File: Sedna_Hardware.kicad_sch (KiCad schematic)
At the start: 24 parts, among them U1 LD1117V33, U2 ESP32-WROOM-32E

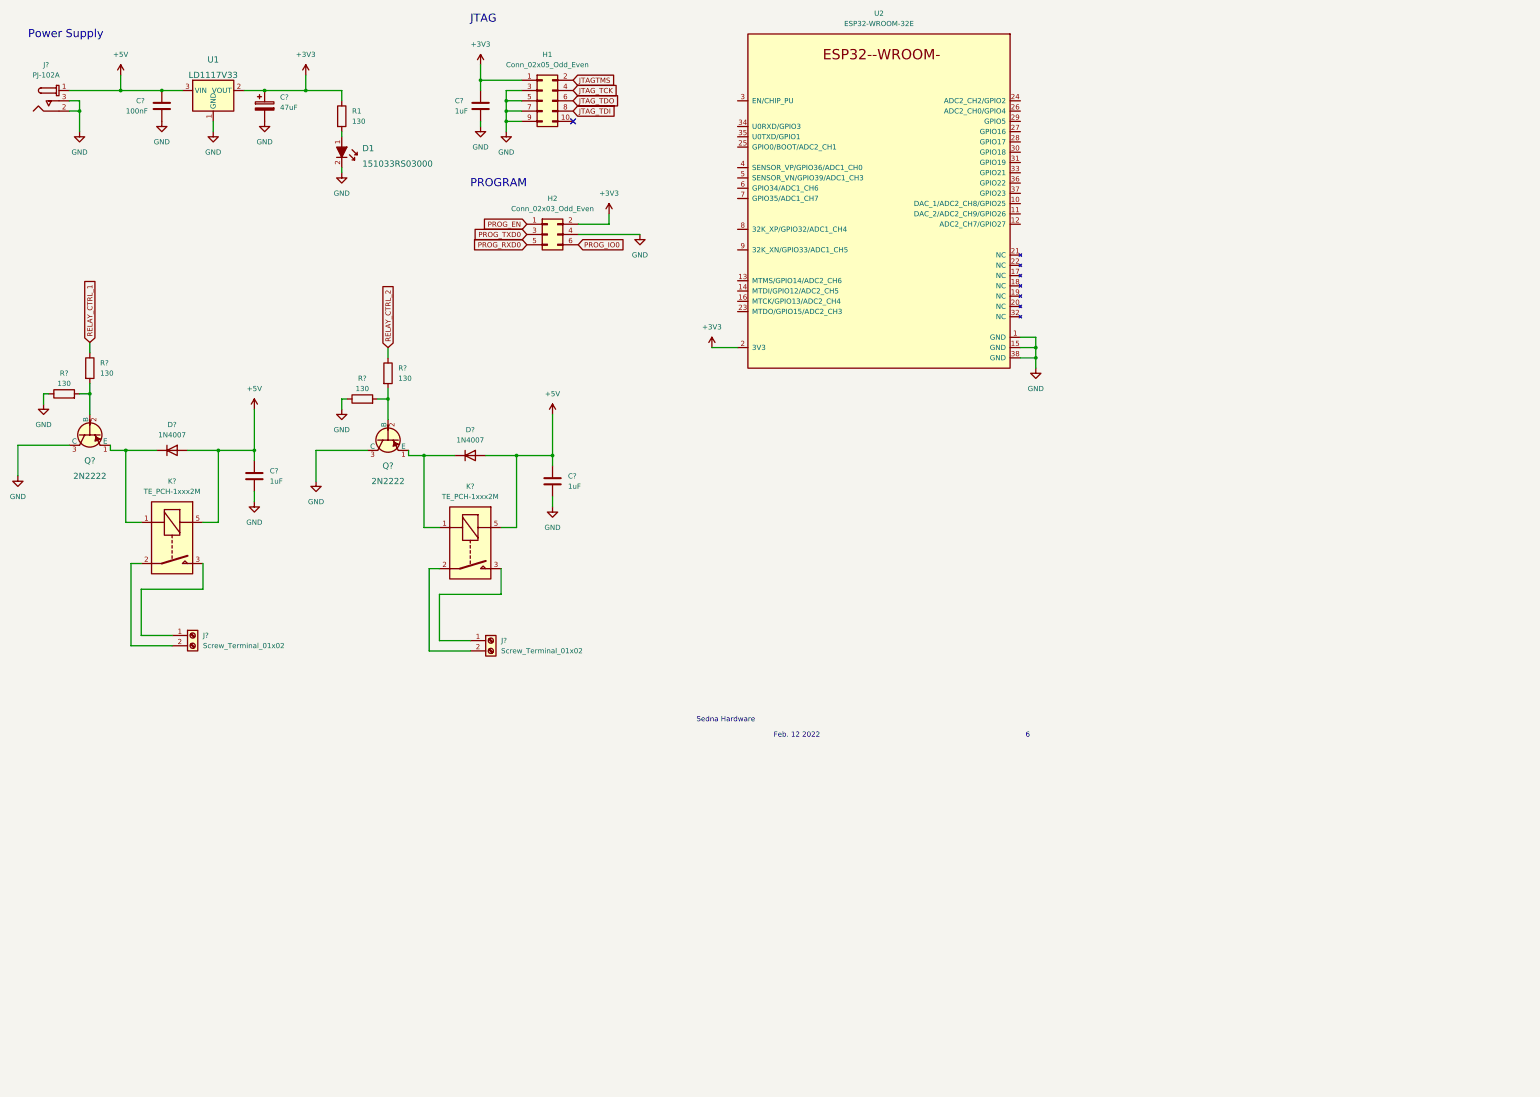
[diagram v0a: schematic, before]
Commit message: Added various headers for sensors, servo, led strips, etc.
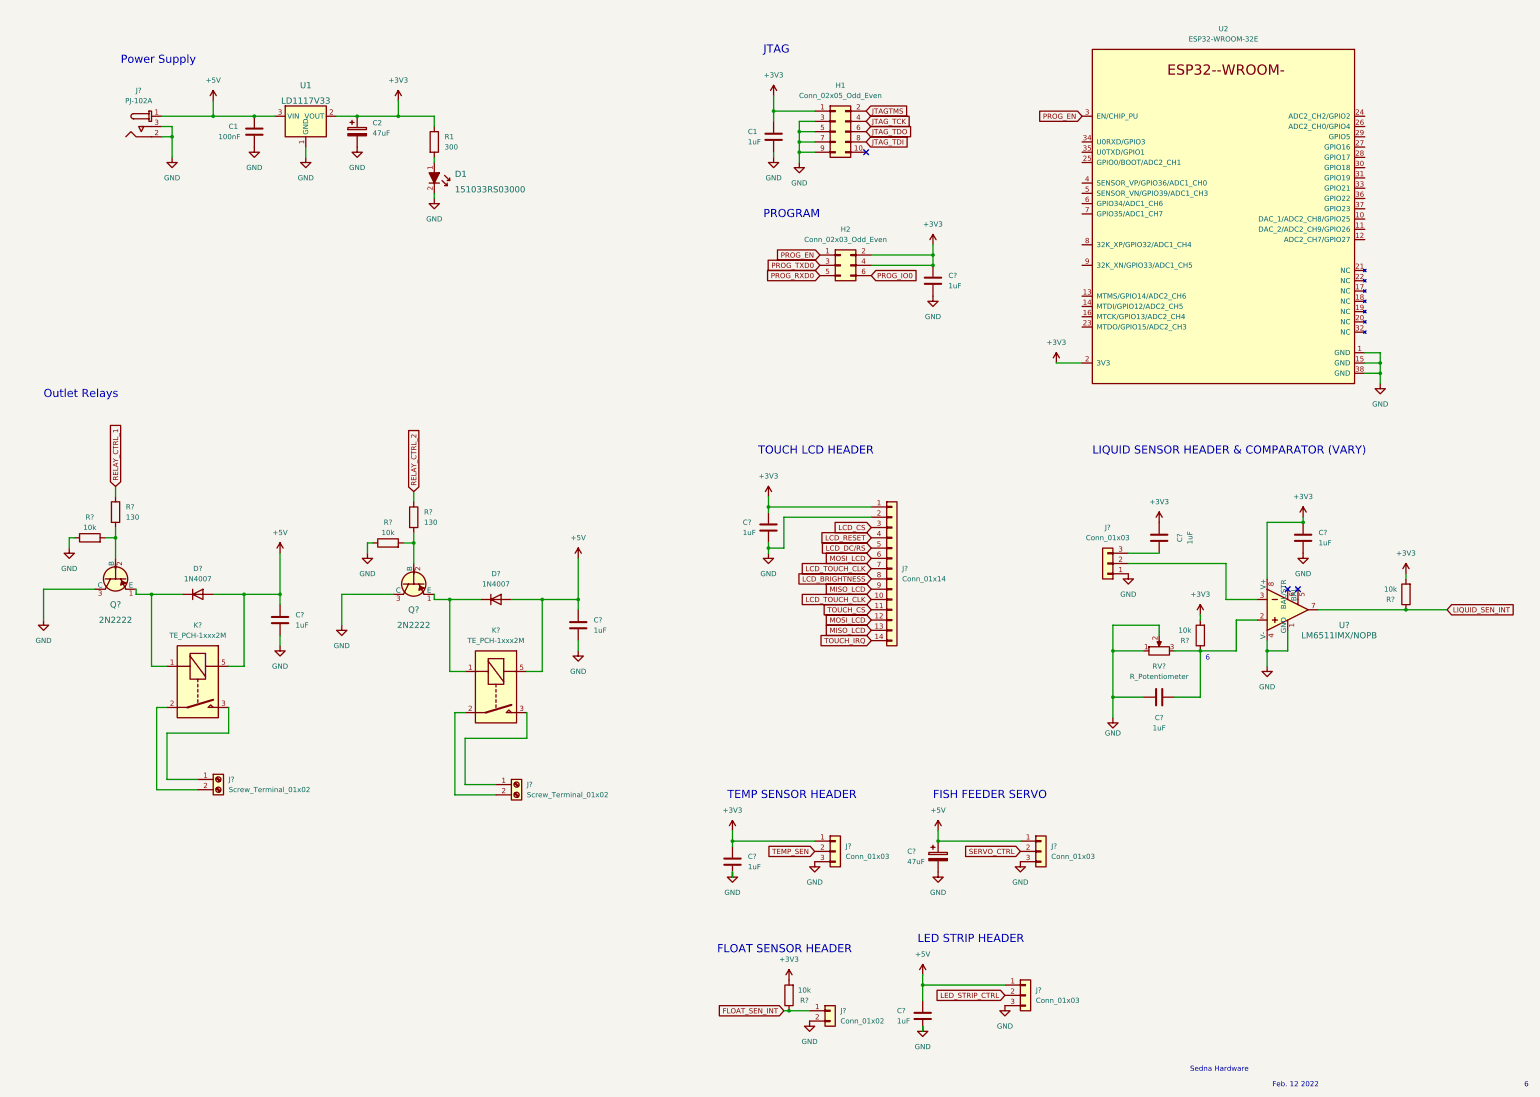
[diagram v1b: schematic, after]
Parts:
- added C? (x7): 1uF, symbol Device:C
- added C?: 47uF, symbol Device:C_Polarized
- added J?: Conn_01x02, symbol Connector_Generic:Conn_01x02
- added J? (x4): Conn_01x03, symbol Connector_Generic:Conn_01x03
- added J?: Conn_01x14, symbol Connector_Generic:Conn_01x14
- added R? (x3): 10k, symbol Device:R
- added RV?: R_Potentiometer, symbol Device:R_Potentiometer
- added U?: LM6511IMX/NOPB, digikey-footprints:DIP-8_W7.62mm, symbol dk_Linear-Comparators:LM311N_NOPB
- R1: value 130 -> 300
- R? (x2): value 130 -> 10k
- gave numbers to parts that had none: 2
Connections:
- net +3V3: now also H2.4 (Pin_4), C?.1, C?.1, C?.1, C?.1, C?.2, J?.1 (Pin_1), J?.1 (Pin_1), R?.2, R?.2, R?.2, U?.8 (V+)
- net +5V: now also C?.1, C?.1, J?.1 (Pin_1), J?.1 (Pin_1)
- net GND: now also C?.1, C?.2, C?.2, C?.2, C?.2, C?.2, C?.2, J?.1 (Pin_1), J?.2 (Pin_2), J?.2 (Pin_2), J?.3 (Pin_3), J?.3 (Pin_3), J?.3 (Pin_3), RV?.1, RV?.2, U?.1 (GND), U?.4 (V-); no longer H2.4 (Pin_4)
- net PROG_EN: now also U2.3 (EN/CHIP_PU)
- new net: C?.1, J?.3 (Pin_3)
- new net: C?.2, R?.1, RV?.3, U?.2
- new net: J?.2 (Pin_2), U?.3
- new net FLOAT_SEN_INT: J?.1 (Pin_1), R?.1
- new net LCD_BRIGHTNESS: J?.8 (Pin_8)
- new net LCD_CS: J?.3 (Pin_3)
- new net LCD_DC/RS: J?.5 (Pin_5)
- new net LCD_RESET: J?.4 (Pin_4)
- new net LCD_TOUCH_CLK: J?.10 (Pin_10), J?.7 (Pin_7)
- new net LED_STRIP_CTRL: J?.2 (Pin_2)
- new net LIQUID_SEN_INT: R?.1, U?.7
- new net MISO_LCD: J?.13 (Pin_13), J?.9 (Pin_9)
- new net MOSI_LCD: J?.12 (Pin_12), J?.6 (Pin_6)
- new net SERVO_CTRL: J?.2 (Pin_2)
- new net TEMP_SEN: J?.2 (Pin_2)
- new net TOUCH_CS: J?.11 (Pin_11)
- new net TOUCH_IRQ: J?.14 (Pin_14)
- no-connect marks 1 -> 3
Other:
- note added: "FISH FEEDER SERVO"
- note added: "FLOAT SENSOR HEADER"
- note added: "LED STRIP HEADER"
- note added: "LIQUID SENSOR HEADER & COMPARATOR (VARY)"
- note added: "Outlet Relays"
- note added: "TEMP SENSOR HEADER"
- note added: "TOUCH LCD HEADER"
- moved on the sheet: C1, C2, C?, D1, D?, H1, H2, J?, K?, Q?, R1, R?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

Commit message: started working on PCB
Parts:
- removed C? (x2): 1uF, symbol Device:C
- removed D? (x2): 1N4007, Diode_THT:D_DO-41_SOD81_P10.16mm_Horizontal, symbol Diode:1N4007
- removed J?: Screw_Terminal_01x02, symbol Connector:Screw_Terminal_01x02
- removed K?: TE_PCH-1xxx2M, Relay_THT:Relay_SPST_TE_PCH-1xxx2M, symbol Relay:TE_PCH-1xxx2M
- removed Q? (x2): 2N2222, digikey-footprints:TO-18-3, symbol dk_Transistors-Bipolar-BJT-Single:2N2222
- removed R?: 10k, symbol Device:R
- removed R?: 130, symbol Device:R
- added C13, C2: 1uF, Capacitor_THT:C_Disc_D9.0mm_W5.0mm_P5.00mm, symbol Device:C
- added C4: 10uF, Capacitor_THT:C_Disc_D9.0mm_W5.0mm_P5.00mm, symbol Device:C
- added D1, D2: 1N4007, Diode_THT:D_DO-41_SOD81_P10.16mm_Horizontal, symbol Diode:1N4007
- added J2: Screw_Terminal_01x02, TerminalBlock:TerminalBlock_Altech_AK300-2_P5.00mm, symbol Connector:Screw_Terminal_01x02
- added K1: ALDP105W, Relay_THT:Relay_SPST_TE_PCH-1xxx2M, symbol Relay:TE_PCH-1xxx2M
- added Q1, Q2: 2N7000-D75Z, digikey-footprints:TO-92-3, symbol dk_Transistors-FETs-MOSFETs-Single:2N7000
- added R1: 100k, Resistor_THT:R_Axial_DIN0204_L3.6mm_D1.6mm_P5.08mm_Horizontal, symbol Device:R
- added R2: 1k, Resistor_THT:R_Axial_DIN0204_L3.6mm_D1.6mm_P5.08mm_Horizontal, symbol Device:R
- added R7: 110, Resistor_THT:R_Axial_DIN0204_L3.6mm_D1.6mm_P5.08mm_Horizontal, symbol Device:R
- added R8: 10k, Resistor_THT:R_Axial_DIN0204_L3.6mm_D1.6mm_P5.08mm_Horizontal, symbol Device:R
- added U?: ESP32-WROOM-32D, RF_Module:ESP32-WROOM-32, symbol RF_Module:ESP32-WROOM-32D
- C1: footprint (none) -> Capacitor_THT:C_Disc_D9.0mm_W5.0mm_P5.00mm
- C10: renamed from C?; footprint (none) -> Capacitor_THT:CP_Radial_D5.0mm_P2.50mm
- C11, C12, C14, C5, C6, C7, C9: renamed from C?; footprint (none) -> Capacitor_THT:C_Disc_D9.0mm_W5.0mm_P5.00mm
- C3: renamed from C2; footprint (none) -> Capacitor_THT:CP_Radial_D5.0mm_P2.50mm
- C8: renamed from C1; footprint (none) -> Capacitor_THT:C_Disc_D9.0mm_W5.0mm_P5.00mm
- J10, J11, J6, J9: renamed from J?; footprint (none) -> Connector_PinHeader_2.54mm:PinHeader_1x03_P2.54mm_Horizontal
- J3: renamed from J?; footprint (none) -> TerminalBlock:TerminalBlock_Altech_AK300-2_P5.00mm
- J4: renamed from J?; footprint (none) -> Connector_PinHeader_2.54mm:PinHeader_1x02_P2.54mm_Horizontal
- J5: renamed from H1; footprint (none) -> Connector_PinHeader_2.54mm:PinHeader_2x05_P2.54mm_Vertical
- J7: renamed from H2; value Conn_02x03_Odd_Even -> 0878340619; footprint (none) -> Connector_PinHeader_2.54mm:PinHeader_2x03_P2.54mm_Vertical; Category (none) -> Rectangular Connectors - Headers, Male Pins; DK_Datasheet_Link (none) -> https://www.molex.com/pdm_docs/sd/878340619_sd.pdf; DK_Detail_Page (none) -> https://www.digikey.ca/en/products/detail/molex/0878340619/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; Digi-Key_PN (none) -> WM14718-ND; MPN (none) -> Molex; Manufacturer (none) -> Molex; Status (none) -> active
- J8: renamed from J?; footprint (none) -> Connector_PinHeader_2.54mm:PinHeader_1x14_P2.54mm_Vertical
- K2: renamed from K?; value TE_PCH-1xxx2M -> ALDP105W; Category (none) -> Relays Power Relays, Over 2 Amps; DK_Datasheet_Link (none) -> https://www3.panasonic.biz/ac/e_download/control/relay/powe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; DK_Detail_Page (none) -> https://www.digikey.ca/en/products/detail/panasonic-electri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; Digi-Key_PN (none) -> 255-3586-ND; MPN (none) -> ALDP105W; Manifacturer (none) -> Panasonic Electric Works; Status (none) -> Active
- R10, R6, R9: renamed from R?; footprint (none) -> Resistor_THT:R_Axial_DIN0204_L3.6mm_D1.6mm_P5.08mm_Horizontal
- R3: renamed from R?; value 10k -> 100k; footprint (none) -> Resistor_THT:R_Axial_DIN0204_L3.6mm_D1.6mm_P5.08mm_Horizontal
- R4: renamed from R?; value 130 -> 1k; footprint (none) -> Resistor_THT:R_Axial_DIN0204_L3.6mm_D1.6mm_P5.08mm_Horizontal
- R5: renamed from R1; footprint (none) -> Resistor_THT:R_Axial_DIN0204_L3.6mm_D1.6mm_P5.08mm_Horizontal
- RV1: renamed from RV?; value R_Potentiometer -> 10k; footprint (none) -> Potentiometer_THT:Potentiometer_Bourns_3296W_Vertical
- U2: Category (none) -> RF Transceiver Modules and Modems; DK_Datasheet_Link (none) -> https://www.espressif.com/sites/default/files/documentation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; DK_Detail_Page (none) -> https://www.digikey.ca/en/products/detail/espressif-systems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; Digi-Key_PN (none) -> 1965-ESP32-WROOM-32E(M113EH6400PH3Q0)DKR-ND; MPN (none) -> ESP32-WROOM-32E(M113EH6400PH3Q0); Manufacturer (none) -> Espressif Systems; Status (none) -> active
- gave numbers to parts that had none: 2
- renumbered D1 to D3
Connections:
- net JTAGTMS is gone; now on net JTAG_TMS: J5.2 (Pin_2)
- net +3V3: now also J11.3 (Pin_3), C13.2, C4.1, U?.2 (VDD); no longer J7.4 (Pin_4)
- net +5V: now also C2.1, D1.1 (K), D2.1 (K), K1.5
- net FLOAT_SEN_INT: now also U2.29 (GPIO5), U?.29 (IO5)
- net GND: now also C13.1, C2.2, C4.2, Q1.1 (S), Q2.1 (S), R1.1, U?.1 (GND), U?.15 (GND), U?.38 (GND), U?.39 (GND)
- net JTAG_TCK: now also U2.16 (MTCK/GPIO13/ADC2_CH4), U?.16 (IO13)
- net JTAG_TDI: now also U2.14 (MTDI/GPIO12/ADC2_CH5), U?.14 (IO12)
- net JTAG_TDO: now also U2.23 (MTDO/GPIO15/ADC2_CH3), U?.23 (IO15)
- net LCD_BRIGHTNESS: now also U2.7 (GPIO35/ADC1_CH7), U?.4 (SENSOR_VP)
- net LCD_CS: now also U2.9 (32K_XN/GPIO33/ADC1_CH5), U?.9 (IO33)
- net LCD_DC/RS: now also U2.6 (GPIO34/ADC1_CH6), U?.6 (IO34)
- net LCD_RESET: now also U2.8 (32K_XP/GPIO32/ADC1_CH4), U?.8 (IO32)
- net LCD_TOUCH_CLK: now also U2.28 (GPIO17), U2.30 (GPIO18), U?.28 (IO17), U?.30 (IO18)
- net LED_STRIP_CTRL: now also U2.11 (DAC_2/ADC2_CH9/GPIO26), U?.11 (IO26)
- net LIQUID_SEN_INT: now also U2.10 (DAC_1/ADC2_CH8/GPIO25), U?.10 (IO25)
- net MISO_LCD: now also U2.31 (GPIO19), U2.36 (GPIO22), U?.31 (IO19), U?.36 (IO22)
- net MOSI_LCD: now also U2.33 (GPIO21), U2.37 (GPIO23), U?.33 (IO21), U?.37 (IO23)
- net PROG_EN: now also U?.3 (EN)
- net PROG_IO0: now also U2.25 (GPIO0/BOOT/ADC2_CH1), U?.25 (IO0)
- net PROG_RXD0: now also U2.34 (U0RXD/GPIO3), U?.34 (RXD0/IO3)
- net PROG_TXD0: now also U2.35 (U0TXD/GPIO1), U?.35 (TXD0/IO1)
- net RELAY_CTRL_1: now also U2.24 (ADC2_CH2/GPIO2), R1.2, R2.1, U?.24 (IO2)
- net RELAY_CTRL_2: now also R3.2, U2.26 (ADC2_CH0/GPIO4), U?.26 (IO4)
- net SERVO_CTRL: now also U2.12 (ADC2_CH7/GPIO27), U?.12 (IO27)
- net TEMP_SEN: now also U2.27 (GPIO16), R7.2, U?.27 (IO16); no longer J6.2 (Pin_2)
- net TOUCH_CS: now also U2.4 (SENSOR_VP/GPIO36/ADC1_CH0), U?.7 (IO35)
- net TOUCH_IRQ: now also U2.5 (SENSOR_VN/GPIO39/ADC1_CH3), U?.5 (SENSOR_VN)
- net at R4.2: now also Q2.2 (G); no longer R3.2
- net at K2.1: now also D2.2 (A), Q2.3 (D)
- net JTAG_TMS: now reaches U2.13 (MTMS/GPIO14/ADC2_CH6)
- net JTAG_TMS: now also U?.13 (IO14)
- net at U3.3: now also R8.1; no longer J11.2 (Pin_2)
- new net: Q1.2 (G), R2.2
- new net: D1.2 (A), K1.1, Q1.3 (D)
- new net: J2.1 (Pin_1), K1.3
- new net: J2.2 (Pin_2), K1.2
- new net: J6.2 (Pin_2), R7.1
- new net: J11.2 (Pin_2), R8.2
- no-connect marks 3 -> 9
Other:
- note added: "ESP32 Controller"
- moved on the sheet: C1, C11, C12, C14, C3, C5, C6, C8, C9, J1, J10, J11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

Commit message: Untangled rat net
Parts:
- removed U2: ESP32-WROOM-32E, Espressif:ESP32-WROOM-32E, symbol Espressif:ESP32-WROOM-32E
- U1: footprint digikey-footprints:TO-220-3 -> Package_TO_SOT_THT:TO-220-3_Horizontal_TabDown
- U2: renamed from U?; value ESP32-WROOM-32D -> ESP32-WROOM-32D-N16
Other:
- moved on the sheet: C8, C9, J5, J7, U2
